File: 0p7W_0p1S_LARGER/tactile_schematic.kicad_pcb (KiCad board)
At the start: 2 copper layers, 145.2 x 85.6 mm, 55 parts, among them IC1 CY8C4145PVI-PS431, J1 Conn_01x03, J2 Conn_01x04, J3 Conn_01x04, J4 Conn_01x03, J5 Conn_ARM_SWD_TagConnect_TC203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

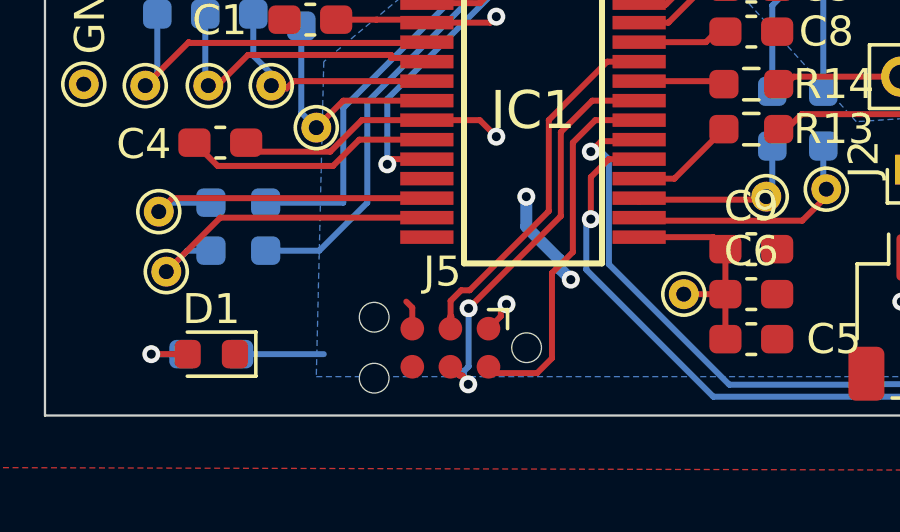
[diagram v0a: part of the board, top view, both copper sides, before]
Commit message: move prog connector up, make bottom of gnd plane connected propelrly
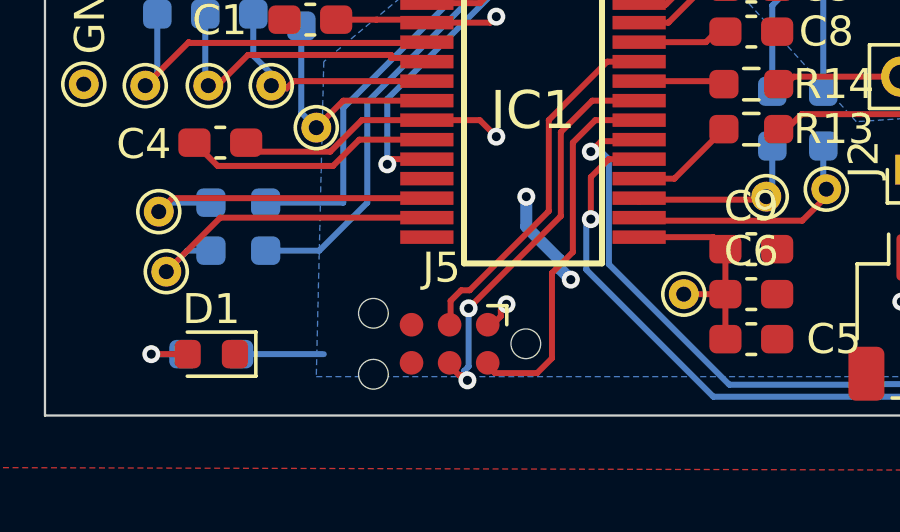
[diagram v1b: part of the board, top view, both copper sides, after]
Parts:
- moved J5 0.13 mm to (111.5, 126.9)
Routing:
- net GND: track 25.4 -> 24.4 mm
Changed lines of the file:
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@@
 	(footprint "Connector:Tag-Connect_TC2030-IDC-NL_2x03_P1.27mm_Vertical"
 		(layer "F.Cu")
-		(at 111.545603 127.031125 180)
+		(at 111.52 126.9 180)
 		(descr "Tag-Connect programming header; http://www.tag-connect.com/Materials/TC2030-IDC-NL.pdf")
 		(tags "tag connect programming header pogo pins")
@@
 			(polygon
 				(pts
-					(xy 110.275603 127.666125) (xy 112.815603 127.666125) (xy 112.815603 126.396125) (xy 110.275603 126.396125)
+					(xy 110.25 127.535) (xy 112.79 127.535) (xy 112.79 126.265) (xy 110.25 126.265)
 				)
 			)
@@
 	)
 	(segment
-		(start 110.275603 125.696125)
-		(end 110.075603 125.496125)
-		(width 0.2)
-		(layer "F.Cu")
-		(net 2)
-	)
-	(segment
 		(start 108.508389 120.096125)
 		(end 107.632389 120.972125)
@@
 		(net 2)
 	)
-	(segment
-		(start 110.275603 126.396125)
-		(end 110.275603 125.696125)
-		(width 0.2)
-		(layer "F.Cu")
-		(net 2)
-	)
 	(via
 		(at 114.075603 121.996125)
@@
 	)
 	(segment
+		(start 112.030092 128.035473)
+		(end 112.019289 128.035473)
+		(width 0.2)
+		(layer "F.Cu")
+		(net 22)
+	)
+	(segment
 		(start 111.844885 127.95772)
 		(end 111.55329 127.666125)
@@
 	)
 	(segment
-		(start 111.941536 127.95772)
-		(end 111.844885 127.95772)
+		(start 112.019289 128.035473)
+		(end 111.941536 127.95772)
 		(width 0.2)
 		(layer "F.Cu")
@@
 	)
 	(segment
-		(start 115.226603 119.845125)
-		(end 116.275603 118.796125)
+		(start 111.55329 127.666125)
+		(end 111.545603 127.666125)
 		(width 0.2)
 		(layer "F.Cu")
@@
 	)
 	(segment
-		(start 115.226603 122.645125)
-		(end 115.226603 119.845125)
+		(start 115.226603 119.845125)
+		(end 116.275603 118.796125)
 		(width 0.2)
 		(layer "F.Cu")
@@
 	)
 	(segment
-		(start 111.55329 127.666125)
-		(end 111.545603 127.666125)
+		(start 115.226603 122.645125)
+		(end 115.226603 119.845125)
 		(width 0.2)
 		(layer "F.Cu")
@@
 	)
 	(segment
-		(start 112.140433 128.156617)
-		(end 111.941536 127.95772)
+		(start 112.11278 128.118161)
+		(end 112.030092 128.035473)
 		(width 0.2)
 		(layer "F.Cu")
@@
 	)
 	(segment
-		(start 112.140433 128.251659)
-		(end 112.140433 128.156617)
+		(start 111.941536 127.95772)
+		(end 111.844885 127.95772)
 		(width 0.2)
 		(layer "F.Cu")
@@
 	)
 	(via
-		(at 112.140433 128.251659)
+		(at 112.11278 128.118161)
 		(size 0.6)
 		(drill 0.3)
@@
 	)
 	(segment
-		(start 112.140433 128.133651)
+		(start 112.042255 128.035473)
 		(end 112 127.993218)
 		(width 0.2)
@@
 	)
 	(segment
-		(start 112 127.993218)
-		(end 112 127.81101)
+		(start 112.042255 128.047636)
+		(end 112.042255 128.035473)
 		(width 0.2)
 		(layer "B.Cu")
@@
 	)
 	(segment
-		(start 112.152973 127.658037)
-		(end 112.152973 125.718755)
+		(start 112 127.81101)
+		(end 112.152973 127.658037)
 		(width 0.2)
 		(layer "B.Cu")
@@
 	)
 	(segment
-		(start 112.140433 128.251659)
-		(end 112.140433 128.133651)
+		(start 112.11278 128.118161)
+		(end 112.042255 128.047636)
 		(width 0.2)
 		(layer "B.Cu")
@@
 	)
 	(segment
-		(start 112 127.81101)
-		(end 112.152973 127.658037)
+		(start 112.152973 127.658037)
+		(end 112.152973 125.718755)
+		(width 0.2)
+		(layer "B.Cu")
+		(net 22)
+	)
+	(segment
+		(start 112 127.993218)
+		(end 112 127.81101)
 		(width 0.2)
 		(layer "B.Cu")
